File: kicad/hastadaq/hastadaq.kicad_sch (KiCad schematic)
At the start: 31 parts, among them J1 HB1 half-bridge #1 (on beam), J2 HB2 half-bridge #2 (on beam), J3 Pitch encoder (MT6835), J4 Pico Plus 2 SP/CE connector (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, J5 SBUS out (V, SIG, GND), J6 Bench PSU in (8.4 V), J7 Trigger IN (from other equip.), J8 Trigger OUT (to other equip.), U1 Pimoroni Pico Plus 2 (header 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, U2 Adafruit ICM20649 IMU (Qwiic,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, U3 Adafruit ADS122C04 #1 (I2C 0x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, U4 Adafruit ADS122C04 #2 (addr j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, U5 Pimoroni RM2 WiFi/BT breakout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, U6 UBEC 5A (set to 5V! input mus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

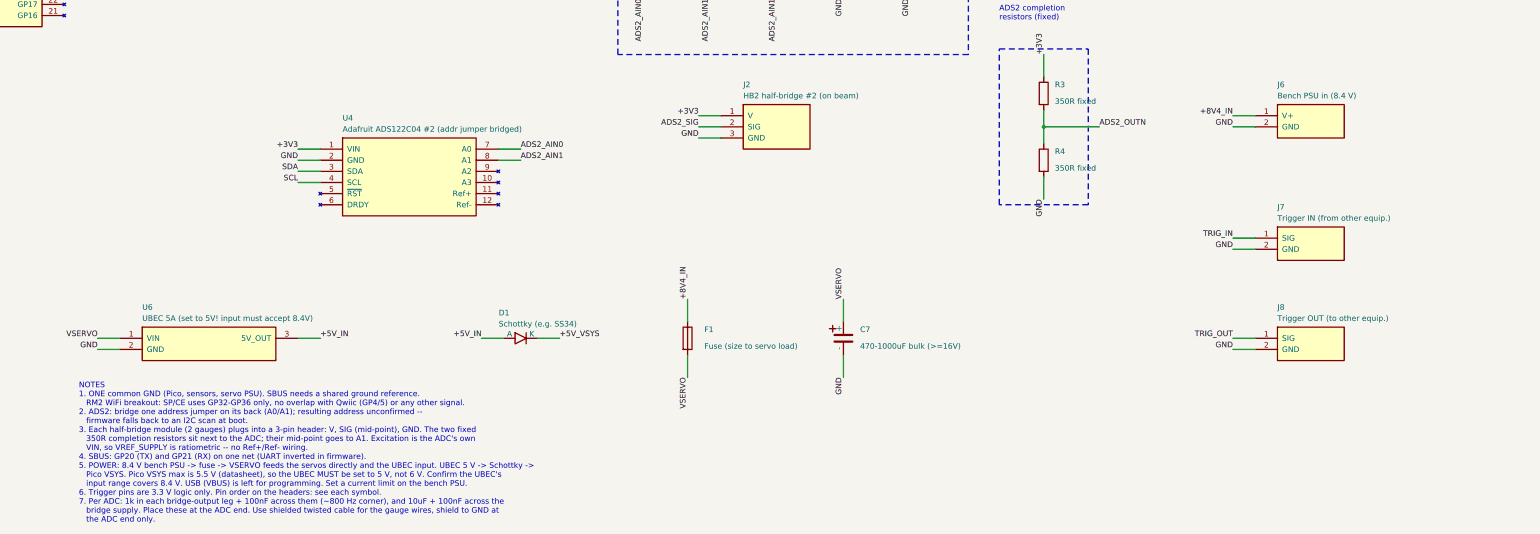
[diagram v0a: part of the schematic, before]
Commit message: HastaDAQ: data classes, test scripts, synchronised moves, power connector
Firmware
- CHANCONFIG accepts an array of channels, validated then applied together
  so several surfaces move in the same SBUS frame (single object still works)

MATLAB
- HastaDaqData: readData() returns an object with a property per servo
  angle (RUDDER_Angle, ...), Time/ServoAngles, ToTable/ToStruct, mean()
- MetaData / ModelConfig for per-test-point context (run/test number, test
  type, model config, ZeroRun, free-form Parameters)
- runNumber.txt helpers (getRunNumber/incrementRunNumber) and getLastZeroRun
- scripts.AoASweep and scripts.ZeroRun collect hdData/ohbData/meta arrays
  per test point and save them; reuse the hd connection between runs
- setAngle sends all surfaces in one command and sends command+JSON in a
  single TCP write; falls back to one-at-a-time on older firmware
- setSteady, example_steady, strain plots in example_chirp

Schematic
- Replace separate PSU/trigger headers with the 8-wire power connector

Co-Authored-By: Claude Sonnet 5.5 <noreply@anthropic.com>
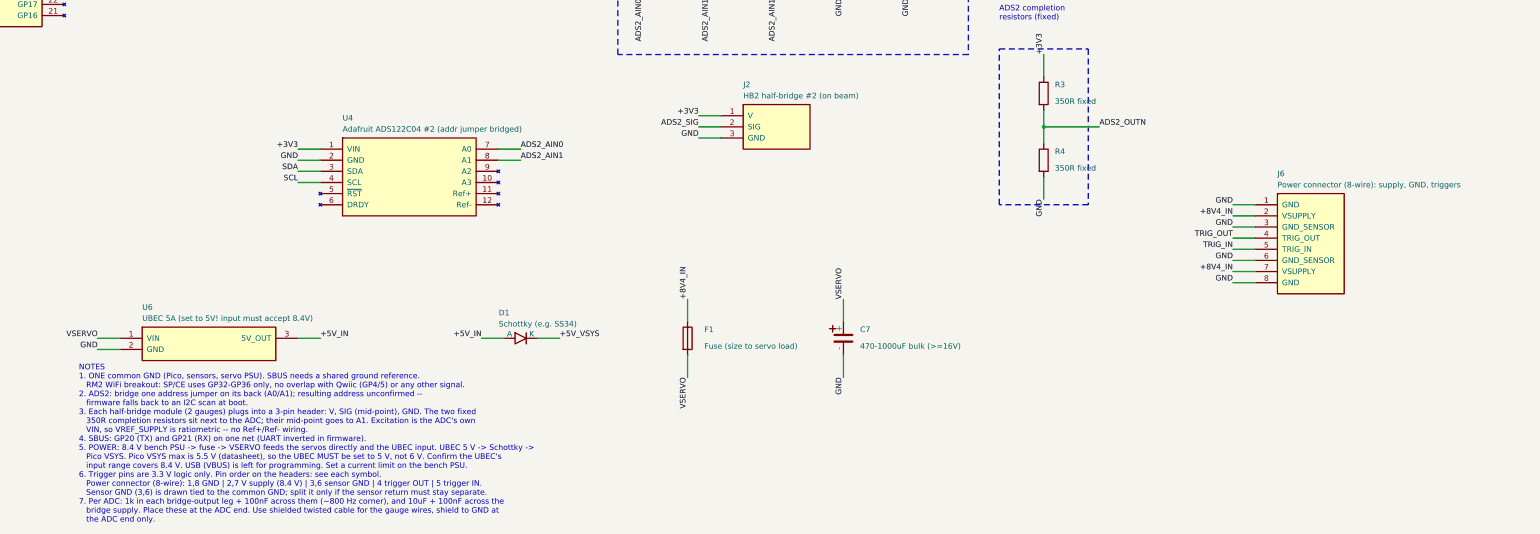
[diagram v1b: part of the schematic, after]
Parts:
- removed J6: Bench PSU in (8.4 V), Connector_PinHeader_2.54mm:PinHeader_1x02_P2.54mm_Vertical, symbol HastaDAQ:Header1x02_VppGND
- removed J7: Trigger IN (from other equip.), Connector_PinHeader_2.54mm:PinHeader_1x02_P2.54mm_Vertical, symbol HastaDAQ:Header1x02_SIGpGND
- removed J8: Trigger OUT (to other equip.), Connector_PinHeader_2.54mm:PinHeader_1x02_P2.54mm_Vertical, symbol HastaDAQ:Header1x02_SIGpGND
- added J6: Power connector (8-wire): supply, GND, triggers, Connector_PinHeader_2.54mm:PinHeader_1x08_P2.54mm_Vertical, symbol HastaDAQ:Header1x08_GNDpVSUPPLYpGNDpSENSORpTRIGpOUTpTRIGpINpGNDpSENSORpVSUPPLYp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
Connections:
- net +8V4_IN: now also J6.2 (VSUPPLY), J6.7 (VSUPPLY)
- net GND: now also J6.1 (GND), J6.3 (GND_SENSOR), J6.6 (GND_SENSOR), J6.8 (GND)
- net TRIG_IN: now also J6.5 (TRIG_IN)
- net TRIG_OUT: now also J6.4 (TRIG_OUT)

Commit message: Schematic rev A: encoders, supply cable, buck modules, trigger I/O
- Four generic 2x4 SPI/encoder headers (CS GP13/9/8/7, pull-ups)
- ADC I2C hard-wired, input filter removed, one shared completion pair
- Single 3x6 SBUS header with a custom HastaDAQ.pretty footprint
- 12 V main supply cable (2x4) with soft-stop loop on GP16
- Pololu D42V55F8 (8.4 V) and SparkFun BabyBuck 5V replace the UBEC
- Opto TRIG_IN and open-drain TRIG_OUT with 3V3/5V/12V pull-up jumper
- IMU via Qwiic-breakout header; RM2 blocks removed (off-board)
- Through-hole footprints throughout; sheet moved to A2
- Docs updated; PDF/PNG re-exported

Co-Authored-By: Claude Sonnet 5.5 <noreply@anthropic.com>
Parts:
- removed C5: 10uF, Capacitor_SMD:C_0805_2012Metric, symbol HastaDAQ:C
- removed C6: 100nF, Capacitor_SMD:C_0805_2012Metric, symbol HastaDAQ:C
- removed C7: 470-1000uF bulk (>=16V), Capacitor_THT:CP_Radial_D10.0mm_P5.00mm, symbol HastaDAQ:C_Polarized
- removed J1: HB1 half-bridge #1 (on beam), Connector_PinHeader_2.54mm:PinHeader_1x03_P2.54mm_Vertical, symbol HastaDAQ:Header1x03_VpSIGpGND
- removed J3: Pitch encoder (MT6835), Connector_PinHeader_2.54mm:PinHeader_1x06_P2.54mm_Vertical, symbol HastaDAQ:Header1x06_GNDpCSpCLKpMOSIpMISOpV
- removed J4: Pico Plus 2 SP/CE connector (8-pin JST-SH), symbol HastaDAQ:SPCE_JST8
- removed J5: SBUS out (V, SIG, GND), Connector_PinHeader_2.54mm:PinHeader_1x03_P2.54mm_Vertical, symbol HastaDAQ:Header1x03_VpSIGpGND
- removed J6: Power connector (8-wire): supply, GND, triggers, Connector_PinHeader_2.54mm:PinHeader_1x08_P2.54mm_Vertical, symbol HastaDAQ:Header1x08_GNDpVSUPPLYpGNDpSENSORpTRIGpOUTpTRIGpINpGNDpSENSORpVSUPPLYp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
- removed U2: Adafruit ICM20649 IMU (Qwiic, 0x68), symbol HastaDAQ:ICM20649
- removed U4: Adafruit ADS122C04 #2 (addr jumper bridged), symbol HastaDAQ:ADS122C04
- removed U5: Pimoroni RM2 WiFi/BT breakout (1:1 JST-SH cable), symbol HastaDAQ:RM2
- removed U6: UBEC 5A (set to 5V! input must accept 8.4V), symbol HastaDAQ:UBEC
- added C5: 100uF input bulk (>=25V), Capacitor_THT:CP_Radial_D8.0mm_P3.50mm, symbol HastaDAQ:C_Polarized
- added C6: 470-1000uF servo bulk (>=16V), Capacitor_THT:CP_Radial_D10.0mm_P5.00mm, symbol HastaDAQ:C_Polarized
- added D2: 1N4148 (LED reverse protect), Diode_THT:D_DO-35_SOD27_P7.62mm_Horizontal, symbol HastaDAQ:D_Schottky
- added J1: IMU via Qwiic breakout (The Pi Hut 106676), Connector_PinHeader_2.54mm:PinHeader_1x04_P2.54mm_Vertical, symbol HastaDAQ:Header1x04_GNDp3V3pSDApSCL
- added J10: TRIG_OUT pull-up sel., Connector_PinHeader_2.54mm:PinHeader_2x03_P2.54mm_Vertical, symbol HastaDAQ:Header2x03_PU_SEL
- added J3: HB2 half-bridge #2 (on beam), Connector_PinHeader_2.54mm:PinHeader_1x03_P2.54mm_Vertical, symbol HastaDAQ:Header1x03_VpSIGpGND
- added J4: ENC1 SPI port: MT6835 (pitch) / Orbis, Connector_PinHeader_2.54mm:PinHeader_2x04_P2.54mm_Vertical, symbol HastaDAQ:Header2x04_GNDpCSpSCKpMOSIpMISOp3V3p5VpGND
- added J5: ENC2 SPI port: MT6835 / Orbis, Connector_PinHeader_2.54mm:PinHeader_2x04_P2.54mm_Vertical, symbol HastaDAQ:Header2x04_GNDpCSpSCKpMOSIpMISOp3V3p5VpGND
- added J6: ENC3 SPI port: MT6835 / Orbis, Connector_PinHeader_2.54mm:PinHeader_2x04_P2.54mm_Vertical, symbol HastaDAQ:Header2x04_GNDpCSpSCKpMOSIpMISOp3V3p5VpGND
- added J7: ENC4 SPI port: generic SPI device, Connector_PinHeader_2.54mm:PinHeader_2x04_P2.54mm_Vertical, symbol HastaDAQ:Header2x04_GNDpCSpSCKpMOSIpMISOp3V3p5VpGND
- added J8: SBUS servo header 3x6 (6 x V, SIG, GND), HastaDAQ:PinHeader_3x06_P2.54mm_Vertical, symbol HastaDAQ:Header3x06_SBUS
- added J9: Main supply cable (2x4): VSUPPLY, VGND, TRIG, SOF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, Connector_PinHeader_2.54mm:PinHeader_2x04_P2.54mm_Vertical, symbol HastaDAQ:Header2x04_VSUPPLYpVGNDpTRIGpINpSOFTSTOPppSOFTSTOPppTRIGpOUTpVGNDpVSUP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
- added Q1: 2N7000 (TO-92: check pinout S/G/D), Package_TO_SOT_THT:TO-92_Inline, symbol HastaDAQ:2N7000
- added R10: 1k 1W, Resistor_THT:R_Axial_DIN0411_L9.9mm_D3.6mm_P12.70mm_Horizontal, symbol HastaDAQ:R
- added R11: 10k pull-up, Resistor_THT:R_Axial_DIN0207_L6.3mm_D2.5mm_P7.62mm_Horizontal, symbol HastaDAQ:R
- added R12: 100R, Resistor_THT:R_Axial_DIN0207_L6.3mm_D2.5mm_P7.62mm_Horizontal, symbol HastaDAQ:R
- added R13: 100k, Resistor_THT:R_Axial_DIN0207_L6.3mm_D2.5mm_P7.62mm_Horizontal, symbol HastaDAQ:R
- added R14: 1.5k pull-up, Resistor_THT:R_Axial_DIN0207_L6.3mm_D2.5mm_P7.62mm_Horizontal, symbol HastaDAQ:R
- added R9: 10k pull-down, Resistor_THT:R_Axial_DIN0207_L6.3mm_D2.5mm_P7.62mm_Horizontal, symbol HastaDAQ:R
- added U2: Adafruit ADS122C04 #1 (I2C 0x40), symbol HastaDAQ:ADS122C04
- added U4: Pololu D42V55F8 8.4V 5A buck (servo rail), Connector_PinHeader_2.54mm:PinHeader_2x06_P2.54mm_Vertical, symbol HastaDAQ:D42V55F8
- added U5: SparkFun BabyBuck 5V (AP63357) (Pico VSYS, Orbis), Connector_PinHeader_2.54mm:PinHeader_1x04_P2.54mm_Vertical, symbol HastaDAQ:BabyBuck_5V
- added U6: PC817 opto (TRIG_IN), Package_DIP:DIP-4_W7.62mm, symbol HastaDAQ:PC817
- C1, C3: value 100nF -> 10uF; footprint Capacitor_SMD:C_0805_2012Metric -> Capacitor_THT:C_Disc_D5.0mm_W2.5mm_P5.00mm
- C2: value 10uF -> 100nF; footprint Capacitor_SMD:C_0805_2012Metric -> Capacitor_THT:C_Disc_D5.0mm_W2.5mm_P5.00mm
- C4: footprint Capacitor_SMD:C_0805_2012Metric -> Capacitor_THT:C_Disc_D5.0mm_W2.5mm_P5.00mm
- D1: value Schottky (e.g. SS34) -> Schottky (e.g. 1N5822, 3A); footprint Diode_SMD:D_SMA -> Diode_THT:D_DO-201AD_P15.24mm_Horizontal
- F1: footprint Fuse:Fuse_1812_4532Metric -> Fuse:Fuseholder_Clip-5x20mm_Keystone_3517_Inline_P23.11x6.76mm_D1.70mm_Horizontal
- J2: value HB2 half-bridge #2 (on beam) -> HB1 half-bridge #1 (on beam)
- R1, R2: footprint Resistor_SMD:R_0805_2012Metric -> Resistor_THT:R_Axial_DIN0207_L6.3mm_D2.5mm_P7.62mm_Horizontal
- R3, R4: value 350R fixed -> 10k; footprint Resistor_SMD:R_0805_2012Metric -> Resistor_THT:R_Axial_DIN0207_L6.3mm_D2.5mm_P7.62mm_Horizontal
- R5, R6: value 1k -> 10k; footprint Resistor_SMD:R_0805_2012Metric -> Resistor_THT:R_Axial_DIN0207_L6.3mm_D2.5mm_P7.62mm_Horizontal
- R7: value 1k -> 1k (soft-stop series); footprint Resistor_SMD:R_0805_2012Metric -> Resistor_THT:R_Axial_DIN0207_L6.3mm_D2.5mm_P7.62mm_Horizontal
- R8: value 1k -> 10k (soft-stop pull-up); footprint Resistor_SMD:R_0805_2012Metric -> Resistor_THT:R_Axial_DIN0207_L6.3mm_D2.5mm_P7.62mm_Horizontal
- U3: value Adafruit ADS122C04 #1 (I2C 0x40) -> Adafruit ADS122C04 #2 (addr jumper bridged)
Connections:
- net +3V3: now also C1.1, C4.1, R4.1, R5.1, R6.1, R8.1, J1.2 (3V3), J10.1 (3V3), J3.1 (V), J4.6 (3V3), J5.6 (3V3), J6.6 (3V3), J7.6 (3V3), R11.1, U2.1 (VIN)
- net ADS1_SIG: now also J2.2 (SIG), U2.7 (A0); no longer R5.1
- net ADS2_SIG: now also U3.7 (A0), J3.2 (SIG); no longer J2.2 (SIG), R7.1
- net GND: now also C1.2, C4.2, C5.2 (-), C6.2 (-), D2.A, J1.1 (GND), J3.3 (GND), J4.1 (GND), J4.8 (GND), J5.1 (GND), J5.8 (GND), J6.1 (GND), J6.8 (GND), J7.1 (GND), J7.8 (GND), J8.12 (S4 GND), J8.15 (S5 GND), J8.18 (S6 GND), J8.3 (S1 GND), J8.6 (S2 GND), J8.9 (S3 GND), J9.2 (VGND), J9.5 (SOFTSTOP-), J9.7 (VGND), Q1.1 (S), R13.2, R9.2, U2.2 (GND), U4.3 (GND), U4.4 (GND), U4.5 (GND), U4.6 (GND), U5.2 (GND), U6.2 (K), U6.3 (E); no longer R4.2
- net SBUS: now also J8.11 (S4 SIG), J8.14 (S5 SIG), J8.17 (S6 SIG), J8.2 (S1 SIG), J8.5 (S2 SIG), J8.8 (S3 SIG)
- net SCL: now also J1.4 (SCL), U2.4 (SCL)
- net SDA: now also J1.3 (SDA), U2.3 (SDA)
- net SPI_MISO: now also J4.5 (MISO), J5.5 (MISO), J6.5 (MISO), J7.5 (MISO)
- net SPI_MOSI: now also J4.4 (MOSI), J5.4 (MOSI), J6.4 (MOSI), J7.4 (MOSI)
- net SPI_SCK: now also J4.3 (SCK), J5.3 (SCK), J6.3 (SCK), J7.3 (SCK)
- net TRIG_IN: now also J9.3 (TRIG_IN), R10.1, R9.1; no longer U1.19 (GP14)
- net TRIG_OUT: now also J9.6 (TRIG_OUT), Q1.3 (D), R14.2; no longer U1.20 (GP15)
- net VSERVO: now also C6.1 (+), J8.1 (S1 V), J8.10 (S4 V), J8.13 (S5 V), J8.16 (S6 V), J8.4 (S2 V), J8.7 (S3 V), U4.1 (VOUT), U4.2 (VOUT); no longer F1.2
- net ENC4_CS: now reaches U1.10 (GP7)
- net ENC4_CS: now also R6.2, J7.2 (CS)
- net ENC3_CS: now reaches U1.11 (GP8)
- net ENC3_CS: now also R5.2, J6.2 (CS)
- net ENC2_CS: now reaches U1.12 (GP9)
- net ENC2_CS: now also R4.2, J5.2 (CS)
- net SOFTSTOP_IN: now reaches U1.21 (GP16)
- net SOFTSTOP_IN: now also R7.2, R8.2
- net +5V_IN renamed +5V
- net +5V: now also J10.3 (5V), J4.7 (5V), J5.7 (5V), J6.7 (5V), J7.7 (5V), U5.1 (VOUT 5V)
- net +8V4_IN renamed +12V_IN
- net +12V_IN: now also J9.1 (VSUPPLY), J9.8 (VSUPPLY)
- removed net ADS1_AIN0: C1.1, R5.2, U3.7 (A0)
- removed net ADS1_AIN1: C1.2, R6.2, U3.8 (A1)
- net ADS1_OUTN renamed ADS_REF
- net ADS_REF: now also U3.8 (A1), U2.8 (A1); no longer R6.1
- removed net ADS2_AIN0: C4.1, R7.2
- removed net ADS2_AIN1: C4.2, R8.2
- removed net ADS2_OUTN: R3.2, R4.1, R8.1
- net SPI_CS renamed ENC1_CS
- net ENC1_CS: now also R3.2, J4.2 (CS)
- new net +12V: C5.1 (+), F1.2, J10.5 (12V), U4.7 (VIN), U4.8 (VIN), U5.3 (VIN), U5.4 (EN)
- new net SOFTSTOP_CABLE: J9.4 (SOFTSTOP+), R7.1
- new net TRIG_IN_GPIO: R11.2, U1.19 (GP14), U6.4 (C)
- new net TRIG_IN_LED: D2.K, R10.2, U6.1 (A)
- new net TRIG_OUT_GATE: Q1.2 (G), R12.2, R13.1
- new net TRIG_OUT_GPIO: R12.1, U1.20 (GP15)
- new net TRIG_PU: J10.2 (PU), J10.4 (PU), J10.6 (PU), R14.1
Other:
- note added: "ADS1 supply decoupling (place at ADC)"
- note added: "ADS2 supply decoupling (place at ADC)"
- note added: "CS pull-ups (10k)"
- note added: "Jumper a row (3V3 / 5V / 12V) to pull TRIG_OUT up to that rail; remove it if the receiver has its own pull-up. Pull-up current: 3.3 V ~2 mA, 5 V ~3 mA, 12 V ~7 mA (enough for a 6.5 mA opto input such as MPS4200). 24 V receivers: no jumper, add an external 24 V pull-up in the harness. 3V3 for eSync 2 high-Z ports (3.3 V max)."
- note added: "NOTES 1. ONE common GND (Pico, sensors, servo PSU). SBUS needs a shared ground reference. RM2 WiFi breakout (off-board, cabled to the Pico Plus 2 SP/CE connector): uses GP32-GP36 only, no overlap with I2C (GP4/5) or any other signal. 2. ADS2: bridge one address jumper on its back (A0/A1); resulting address unconfirmed -- firmware falls back to an I2C scan at boot. I2C pull-ups: rely on the Adafru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"
- note added: "Pimoroni Pico Plus 2 (+ RM2 on SP/CE): same 40-pin header as Pico 2 W. I2C0 = GP4/GP5 (header pins 6/7), hard-wired to the IMU Qwiic-breakout header and both ADS122C04 boards by header pins. Crossed-out pins are intentionally unused."
- note added: "Shared completion resistors (fixed) -> A1 of BOTH ADCs"
- note added: "TRIGGER IN: any 3.3 V .. 24 V level, opto input"
- note added: "TRIGGER OUT: open-drain, pull-up rail chosen by jumper"
- note removed: "ADS1 completion resistors (fixed)"
- note removed: "ADS1 input filter + supply decoupling (place at ADC)"
- note removed: "ADS2 completion resistors (fixed)"
- note removed: "ADS2 input filter + supply decoupling (place at ADC)"
- note removed: "NOTES 1. ONE common GND (Pico, sensors, servo PSU). SBUS needs a shared ground reference. RM2 WiFi breakout: SP/CE uses GP32-GP36 only, no overlap with Qwiic (GP4/5) or any other signal. 2. ADS2: bridge one address jumper on its back (A0/A1); resulting address unconfirmed -- firmware falls back to an I2C scan at boot. 3. Each half-bridge module (2 gauges) plugs into a 3-pin header: V, SIG (mid-po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"
- note removed: "Pimoroni Pico Plus 2 (+ RM2 on SP/CE): same 40-pin header as Pico 2 W. Qwiic port = GP4/GP5 (I2C0), same nets as header pins 6/7 and 3V3 as pin 36. Each ADS122C04 board also has two Qwiic connectors in parallel with its VIN/GND/SDA/SCL pins. Crossed-out pins are intentionally unused."

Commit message: Schematic: footprints, pin types, protection and test points; module footprints
Assign real footprints (Pico, ADS122C04, Pololu, BabyBuck, Qwiic socket with 3D
model, keyed IDC headers), set electrical pin types with PWR_FLAGs (ERC 0),
servo header GND/V/SIG, soft-stop zener, 5V bulk cap, BabyBuck EN left open,
fuse value, two GND test points. Add generate_module_footprints.py.

Co-Authored-By: Claude Sonnet 5.5 <noreply@anthropic.com>
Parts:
- removed D2: 1N4148 (LED reverse protect), Diode_THT:D_DO-35_SOD27_P7.62mm_Horizontal, symbol HastaDAQ:D_Schottky
- removed Q1: 2N7000 (TO-92: check pinout S/G/D), Package_TO_SOT_THT:TO-92_Inline, symbol HastaDAQ:2N7000
- added C7: 100uF 5V bulk (>=10V), Capacitor_THT:CP_Radial_D6.3mm_P2.50mm, symbol HastaDAQ:C_Polarized
- added D2: 5.1V zener (BZX55C5V1) soft-stop clamp, Diode_THT:D_DO-35_SOD27_P7.62mm_Horizontal, symbol HastaDAQ:D_Zener
- added D3: 1N4148 (LED reverse protect), Diode_THT:D_DO-35_SOD27_P7.62mm_Horizontal, symbol HastaDAQ:D_Schottky
- added Q1: 2N3904 NPN (TO-92, pin 1 E, 2 B, 3 C), Package_TO_SOT_THT:TO-92_Inline, symbol HastaDAQ:2N3904
- added TP1, TP2: TP, TestPoint:TestPoint_THTPad_D2.0mm_Drill1.0mm, symbol HastaDAQ:TestPoint
- F1: value Fuse (size to servo load) -> Fuse T3.15A 5x20mm time-delay
- J1: footprint Connector_PinHeader_2.54mm:PinHeader_1x04_P2.54mm_Vertical -> HastaDAQ:Qwiic_Breakout_1x4_Socket
- J4, J5, J6, J7, J9: footprint Connector_PinHeader_2.54mm:PinHeader_2x04_P2.54mm_Vertical -> Connector_IDC:IDC-Header_2x04_P2.54mm_Vertical
- J8: value SBUS servo header 3x6 (6 x V, SIG, GND) -> SBUS servo header 3x6 (6 plugs: GND, V, SIG)
- R12: value 100R -> 2.2k (base)
- R13: value 100k -> 10k (base-emitter)
- U1: footprint (none) -> Module:RaspberryPi_Pico_Common_THT
- U2, U3: footprint (none) -> HastaDAQ:Adafruit_ADS122C04_Breakout
- U4: footprint Connector_PinHeader_2.54mm:PinHeader_2x06_P2.54mm_Vertical -> HastaDAQ:Pololu_D42V55Fx
- U5: footprint Connector_PinHeader_2.54mm:PinHeader_1x04_P2.54mm_Vertical -> HastaDAQ:SparkFun_BabyBuck_5V
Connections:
- net +12V: no longer U5.4 (EN)
- net +5V: now also C7.1 (+)
- net GND: now also J8.1 (S1 GND), J8.10 (S4 GND), J8.13 (S5 GND), J8.16 (S6 GND), J8.4 (S2 GND), J8.7 (S3 GND), C7.2 (-), D2.A, D3.A, Q1.1 (E), TP1.1, TP2.1; no longer J8.12 (S4 GND), J8.15 (S5 GND), J8.18 (S6 GND), J8.3 (S1 GND), J8.6 (S2 GND), J8.9 (S3 GND)
- net SBUS: now also J8.12 (S4 SIG), J8.15 (S5 SIG), J8.18 (S6 SIG), J8.3 (S1 SIG), J8.6 (S2 SIG), J8.9 (S3 SIG); no longer J8.11 (S4 SIG), J8.14 (S5 SIG), J8.17 (S6 SIG), J8.2 (S1 SIG), J8.5 (S2 SIG), J8.8 (S3 SIG)
- net SOFTSTOP_IN: now also D2.K
- net TRIG_IN_LED: now also D3.K
- net TRIG_OUT: now also Q1.3 (C)
- net VSERVO: now also J8.11 (S4 V), J8.14 (S5 V), J8.17 (S6 V), J8.2 (S1 V), J8.5 (S2 V), J8.8 (S3 V); no longer J8.1 (S1 V), J8.10 (S4 V), J8.13 (S5 V), J8.16 (S6 V), J8.4 (S2 V), J8.7 (S3 V)
- net TRIG_OUT_GATE renamed TRIG_OUT_BASE
- net TRIG_OUT_BASE: now also Q1.2 (B)
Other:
- note added: "PWR_FLAG: marks nets supplied through the supply connector (+12V_IN, GND), the fuse (+12V) and the Schottky (+5V_VSYS)"
- note added: "TEST POINTS (2.0 mm through-hole pads): two GND pads for a scope clip (near the supply and near the ADCs). Rails and signals are probed at component leads and header pins (fuse clips, C5/C6/C7, D1, Pico pins 36/39)."
- note added: "TRIGGER OUT: open-collector NPN, pull-up rail chosen by jumper"
- note removed: "TRIGGER OUT: open-drain, pull-up rail chosen by jumper"

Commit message: Split strain-gauge hardware onto its own board; SBUS IN header; gauge loom diagram
- kicad/gaugeboard: new schematic with 2x ADS122C04, half-bridge headers, shared
  350R completion pair, optional input filter and its own LP2950-N 3.3 V LDO,
  fed from 5 V over a 4-wire I2C loom (GND, +5V, SDA, SCL)
- Main board: strain-gauge circuitry replaced by the 1x4 loom header (J2);
  SBUS_IN 3-pin header on GP1; refs renumbered
- Shared generator helpers in kicad/tools/schgen_common.py; new generate_gauge_sch.py
- Docs: PCB_BRIEF.md rewritten for the main board, new PCB_BRIEF_GAUGE.md, README updated
- wiring/gauge-loom.yml: WireViz diagram of the loom
- HastaDAQ_v2 comments updated for the two-board hardware

Co-Authored-By: Claude Sonnet 5.5 <noreply@anthropic.com>
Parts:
- removed C1, C3: 10uF, Capacitor_THT:C_Disc_D5.0mm_W2.5mm_P5.00mm, symbol HastaDAQ:C
- removed C2, C4: 100nF, Capacitor_THT:C_Disc_D5.0mm_W2.5mm_P5.00mm, symbol HastaDAQ:C
- removed C5: 100uF input bulk (>=25V), Capacitor_THT:CP_Radial_D8.0mm_P3.50mm, symbol HastaDAQ:C_Polarized
- removed C6: 470-1000uF servo bulk (>=16V), Capacitor_THT:CP_Radial_D10.0mm_P5.00mm, symbol HastaDAQ:C_Polarized
- removed C7: 100uF 5V bulk (>=10V), Capacitor_THT:CP_Radial_D6.3mm_P2.50mm, symbol HastaDAQ:C_Polarized
- removed J10: TRIG_OUT pull-up sel., Connector_PinHeader_2.54mm:PinHeader_2x03_P2.54mm_Vertical, symbol HastaDAQ:Header2x03_PU_SEL
- removed J2: HB1 half-bridge #1 (on beam), Connector_PinHeader_2.54mm:PinHeader_1x03_P2.54mm_Vertical, symbol HastaDAQ:Header1x03_VpSIGpGND
- removed J3: HB2 half-bridge #2 (on beam), Connector_PinHeader_2.54mm:PinHeader_1x03_P2.54mm_Vertical, symbol HastaDAQ:Header1x03_VpSIGpGND
- removed J7: ENC4 SPI port: generic SPI device, Connector_IDC:IDC-Header_2x04_P2.54mm_Vertical, symbol HastaDAQ:Header2x04_GNDpCSpSCKpMOSIpMISOp3V3p5VpGND
- removed J8: SBUS servo header 3x6 (6 plugs: GND, V, SIG), HastaDAQ:PinHeader_3x06_P2.54mm_Vertical, symbol HastaDAQ:Header3x06_SBUS
- removed J9: Main supply cable (2x4): VSUPPLY, VGND, TRIG, SOF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, Connector_IDC:IDC-Header_2x04_P2.54mm_Vertical, symbol HastaDAQ:Header2x04_VSUPPLYpVGNDpTRIGpINpSOFTSTOPppSOFTSTOPppTRIGpOUTpVGNDpVSUP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
- removed U2: Adafruit ADS122C04 #1 (I2C 0x40), HastaDAQ:Adafruit_ADS122C04_Breakout, symbol HastaDAQ:ADS122C04
- removed U3: Adafruit ADS122C04 #2 (addr jumper bridged), HastaDAQ:Adafruit_ADS122C04_Breakout, symbol HastaDAQ:ADS122C04
- removed U4: Pololu D42V55F8 8.4V 5A buck (servo rail), HastaDAQ:Pololu_D42V55Fx, symbol HastaDAQ:D42V55F8
- removed U5: SparkFun BabyBuck 5V (AP63357) (Pico VSYS, Orbis), HastaDAQ:SparkFun_BabyBuck_5V, symbol HastaDAQ:BabyBuck_5V
- removed U6: PC817 opto (TRIG_IN), Package_DIP:DIP-4_W7.62mm, symbol HastaDAQ:PC817
- added C1: 100uF input bulk (>=25V), Capacitor_THT:CP_Radial_D8.0mm_P3.50mm, symbol HastaDAQ:C_Polarized
- added C2: 470-1000uF servo bulk (>=16V), Capacitor_THT:CP_Radial_D10.0mm_P5.00mm, symbol HastaDAQ:C_Polarized
- added C3: 100uF 5V bulk (>=10V), Capacitor_THT:CP_Radial_D6.3mm_P2.50mm, symbol HastaDAQ:C_Polarized
- added J10: SBUS IN (RC receiver): GND, V, SIG, Connector_PinHeader_2.54mm:PinHeader_1x03_P2.54mm_Vertical, symbol HastaDAQ:Header1x03_GNDpVpSIG
- added J2: GAUGE BOARD LOOM (J_I2C): GND, +5V, SDA, SCL, Connector_PinHeader_2.54mm:PinHeader_1x04_P2.54mm_Vertical, symbol HastaDAQ:Header1x04_GNDp5VpSDApSCL
- added J3: ENC1 SPI port: MT6835 (pitch) / Orbis, Connector_IDC:IDC-Header_2x04_P2.54mm_Vertical, symbol HastaDAQ:Header2x04_GNDpCSpSCKpMOSIpMISOp3V3p5VpGND
- added J7: SBUS servo header 3x6 (6 plugs: GND, V, SIG), HastaDAQ:PinHeader_3x06_P2.54mm_Vertical, symbol HastaDAQ:Header3x06_SBUS
- added J8: Main supply cable (2x4): VSUPPLY, VGND, TRIG, SOF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, Connector_IDC:IDC-Header_2x04_P2.54mm_Vertical, symbol HastaDAQ:Header2x04_VSUPPLYpVGNDpTRIGpINpSOFTSTOPppSOFTSTOPppTRIGpOUTpVGNDpVSUP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
- added J9: TRIG_OUT pull-up sel., Connector_PinHeader_2.54mm:PinHeader_2x03_P2.54mm_Vertical, symbol HastaDAQ:Header2x03_PU_SEL
- added U2: Pololu D42V55F8 8.4V 5A buck (servo rail), HastaDAQ:Pololu_D42V55Fx, symbol HastaDAQ:D42V55F8
- added U3: SparkFun BabyBuck 5V (AP63357) (Pico VSYS, Orbis), HastaDAQ:SparkFun_BabyBuck_5V, symbol HastaDAQ:BabyBuck_5V
- added U4: PC817 opto (TRIG_IN), Package_DIP:DIP-4_W7.62mm, symbol HastaDAQ:PC817
- J4: value ENC1 SPI port: MT6835 (pitch) / Orbis -> ENC2 SPI port: MT6835 / Orbis
- J5: value ENC2 SPI port: MT6835 / Orbis -> ENC3 SPI port: MT6835 / Orbis
- J6: value ENC3 SPI port: MT6835 / Orbis -> ENC4 SPI port: generic SPI device
- R1, R2: value 350R fixed -> 10k
- R10: value 1k 1W -> 2.2k (base); footprint Resistor_THT:R_Axial_DIN0411_L9.9mm_D3.6mm_P12.70mm_Horizontal -> Resistor_THT:R_Axial_DIN0207_L6.3mm_D2.5mm_P7.62mm_Horizontal
- R11: value 10k pull-up -> 10k (base-emitter)
- R12: value 2.2k (base) -> 1.5k pull-up
- R13: value 10k (base-emitter) -> 1k series
- R14: value 1.5k pull-up -> 10k pull-down
- R5: value 10k -> 1k (soft-stop series)
- R6: value 10k -> 10k (soft-stop pull-up)
- R7: value 1k (soft-stop series) -> 10k pull-down
- R8: value 10k (soft-stop pull-up) -> 1k 1W; footprint Resistor_THT:R_Axial_DIN0207_L6.3mm_D2.5mm_P7.62mm_Horizontal -> Resistor_THT:R_Axial_DIN0411_L9.9mm_D3.6mm_P12.70mm_Horizontal
- R9: value 10k pull-down -> 10k pull-up
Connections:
- net +12V: now also C1.1 (+), J9.5 (12V), U2.7 (VIN), U2.8 (VIN), U3.3 (VIN)
- net +12V_IN: now also J8.1 (VSUPPLY), J8.8 (VSUPPLY)
- net +3V3: now also R2.1, R9.1, J3.6 (3V3), J9.1 (3V3); no longer R11.1, R5.1, R8.1
- net +5V: now also C3.1 (+), J2.2 (5V), J3.7 (5V), J9.3 (5V), U3.1 (VOUT 5V)
- net ENC1_CS: now also R1.2, J3.2 (CS); no longer J4.2 (CS), R3.2
- net ENC2_CS: now also J4.2 (CS), R2.2; no longer J5.2 (CS), R4.2
- net ENC3_CS: now also J5.2 (CS), R3.2; no longer J6.2 (CS), R5.2
- net ENC4_CS: now also J6.2 (CS), R4.2; no longer R6.2
- net GND: now also R11.2, R14.2, R7.2, C1.2 (-), C2.2 (-), C3.2 (-), J10.1 (GND), J2.1 (GND), J3.1 (GND), J3.8 (GND), J7.1 (S1 GND), J7.10 (S4 GND), J7.13 (S5 GND), J7.16 (S6 GND), J7.4 (S2 GND), J7.7 (S3 GND), J8.2 (VGND), J8.5 (SOFTSTOP-), J8.7 (VGND), U2.3 (GND), U2.4 (GND), U2.5 (GND), U2.6 (GND), U3.2 (GND), U4.2 (K), U4.3 (E); no longer R13.2, R2.2, R9.2
- net SBUS: now also J7.12 (S4 SIG), J7.15 (S5 SIG), J7.18 (S6 SIG), J7.3 (S1 SIG), J7.6 (S2 SIG), J7.9 (S3 SIG)
- net SCL: now also J2.4 (SCL)
- net SDA: now also J2.3 (SDA)
- net SOFTSTOP_CABLE: now also R5.1, J8.4 (SOFTSTOP+); no longer R7.1
- net SOFTSTOP_IN: now also R5.2, R6.2; no longer R7.2, R8.2
- net SPI_MISO: now also J3.5 (MISO)
- net SPI_MOSI: now also J3.4 (MOSI)
- net SPI_SCK: now also J3.3 (SCK)
- net TRIG_IN: now also R7.1, R8.1, J8.3 (TRIG_IN); no longer R10.1, R9.1
- net TRIG_IN_GPIO: now also R9.2, U4.4 (C); no longer R11.2
- net TRIG_IN_LED: now also R8.2, U4.1 (A); no longer R10.2
- net TRIG_OUT: now also R12.2, J8.6 (TRIG_OUT); no longer R14.2
- net TRIG_OUT_BASE: now also R10.2, R11.1; no longer R12.2, R13.1
- net TRIG_OUT_GPIO: now also R10.1; no longer R12.1
- net TRIG_PU: now also R12.1, J9.2 (PU), J9.4 (PU), J9.6 (PU); no longer R14.1
- net VSERVO: now also C2.1 (+), J10.2 (V), J7.11 (S4 V), J7.14 (S5 V), J7.17 (S6 V), J7.2 (S1 V), J7.5 (S2 V), J7.8 (S3 V), U2.1 (VOUT), U2.2 (VOUT)
- net SBUS_IN_GPIO: now reaches U1.2 (GP1 UART0-RX)
- net SBUS_IN_GPIO: now also R13.2, R14.1
- removed net ADS_REF: R1.2, R2.1
- new net SBUS_IN: J10.3 (SIG), R13.1
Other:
- note added: "NOTES 1. ONE common GND (Pico, sensors, servo PSU). SBUS needs a shared ground reference. RM2 WiFi breakout (off-board, cabled to the Pico Plus 2 SP/CE connector): uses GP32-GP36 only, no overlap with I2C (GP4/5) or any other signal. 2. Strain gauges: SEPARATE board (kicad/gaugeboard), reached by a 4-wire I2C loom (GND, +5V, SDA, SCL; 0.1in headers, keyed plugs). That board makes its own clean 3.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"
- note added: "Pimoroni Pico Plus 2 (+ RM2 on SP/CE): same 40-pin header as Pico 2 W. I2C0 = GP4/GP5 (header pins 6/7), to the IMU Qwiic-breakout header and to the 4-wire loom for the strain-gauge board. Crossed-out pins are intentionally unused."
- note added: "SBUS IN: RC-receiver pass-through (plug order GND, V, SIG). V = VSERVO 8.4 V -- check the receiver's max supply. SIG -> 1k -> GP1 (UART0 RX), 10k to GND."
- note added: "Strain-gauge board: 4-wire I2C loom. Pin 2 is +5V, NOT 3V3 -- use a keyed plug, never a Qwiic cable. Pull-ups live on the ADS122C04 breakouts on that board."
- note added: "TEST POINTS (2.0 mm through-hole pads): two GND pads for a scope clip (near the supply and near the Pico). Rails and signals are probed at component leads and header pins (fuse clips, C5/C6/C7, D1, Pico pins 36/39)."
- note removed: "ADS1 supply decoupling (place at ADC)"
- note removed: "ADS2 supply decoupling (place at ADC)"
- note removed: "NOTES 1. ONE common GND (Pico, sensors, servo PSU). SBUS needs a shared ground reference. RM2 WiFi breakout (off-board, cabled to the Pico Plus 2 SP/CE connector): uses GP32-GP36 only, no overlap with I2C (GP4/5) or any other signal. 2. ADS2: bridge one address jumper on its back (A0/A1); resulting address unconfirmed -- firmware falls back to an I2C scan at boot. I2C pull-ups: rely on the Adafru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"
- note removed: "Pimoroni Pico Plus 2 (+ RM2 on SP/CE): same 40-pin header as Pico 2 W. I2C0 = GP4/GP5 (header pins 6/7), hard-wired to the IMU Qwiic-breakout header and both ADS122C04 boards by header pins. Crossed-out pins are intentionally unused."
- note removed: "Shared completion resistors (fixed) -> A1 of BOTH ADCs"
- note removed: "TEST POINTS (2.0 mm through-hole pads): two GND pads for a scope clip (near the supply and near the ADCs). Rails and signals are probed at component leads and header pins (fuse clips, C5/C6/C7, D1, Pico pins 36/39)."
